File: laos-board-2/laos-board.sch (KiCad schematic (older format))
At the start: 94 parts, among them IC1 KB847, IC2 KB847, J1 USB-A, J10 CONN_4, J11 MBED NXP, J12 JP, J13 JP_3, J14 CONN_4, J15 JP, J16 JP_3, J17 POLOLU1201, J18 CONN_5, J19 JP, J2 CONN_4, J20 JP_3, J21 JP, J22 JP_3, J23 POLOLU1201, J24 CONN_5, J25 JP, J26 JP_3, J27 CONN_4, J28 JP3, J29 CONN_4, J3 JP, J30 JP, J31 JP_3, J32 POLOLU1201, J33 CONN_5, J34 CONN_4, J35 JP, J36 JP_3, J37 CONN_4, J38 CONN_2, J39 CONN_4, J4 MAGJACK, J5 CONN_2, J6 JP, J7 JP_3, J8 POLOLU1201, J9 CONN_5, Q1 TIP115, Q2 TIP115, U1 65HVD251, U2 SDCARD, U3 7805

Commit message: some more rev2 changes
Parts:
- gave numbers to parts that had none: 1
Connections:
- net GND: no longer J1.GND
- net at J11.20 (P1.31/SCK1/AD0.5), J11.24 (P2.2/PWM1.3/CTS1), J23.7 (STEP): now also J26.3 (P2)
- net at IC2.4, J11.21 (P2.5/PWM1.6/DTR1), J32.7 (STEP): now also J36.3 (P2)
- net at IC2.2, J11.22 (P2.4/PWM1.5/DSR1), J32.8 (DIR): now also J36.5 (P3)
- net at J11.23 (P2.3/PWM1.4/DCD1), J23.8 (DIR): now also J26.5 (P3)
- net at J11.26 (P2.0/PWM1.1/TXD1), J17.7 (STEP): now also J20.3 (P2)
- net at D1.2 (K), J11.7 (P0.7/SCK1/MAT2.1), J17.1 (/ENABLE)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: now also J26.1 (P1), J36.1 (P1)
- net at J31.2 (P6): now also J32.2 (MS1)
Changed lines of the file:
@@
-EESchema Schematic File Version 2  date Tue 20 Sep 2011 03:51:02 PM CEST
+EESchema Schematic File Version 2  date Wed 21 Sep 2011 02:04:42 PM CEST
 LIBS:laos_kicad_lib
 LIBS:laos-board-cache
@@
 Sheet 1 1
 Title "LAOS"
-Date "20 sep 2011"
-Rev "1"
+Date "21 sep 2011"
+Rev "2"
 Comp "http://www.laoslaser.org"
 Comment1 ""
@@
 Comment4 ""
 $EndDescr
-$Comp
-L VAA #PWR?
-U 1 1 4E7898E1
-P 11440 1440
-F 0 "#PWR?" H 11440 1500 30  0001 C CNN
-F 1 "VAA" H 11440 1550 30  0000 C CNN
-	1    11440 1440
-	1    0    0    -1
-$EndComp
+Wire Wire Line
+	7150 1020 7150 1225
+Wire Wire Line
+	12000 2600 12000 1945
+Wire Wire Line
+	11440 1435 11440 1560
+Connection ~ 9045 8625
+Wire Wire Line
+	9045 8625 9045 9150
+Wire Wire Line
+	9045 9150 10250 9150
+Wire Wire Line
+	9300 8125 8650 8125
+Connection ~ 9020 6800
+Wire Wire Line
+	9020 6800 9020 7330
+Wire Wire Line
+	9020 7330 10250 7325
+Connection ~ 9095 5050
+Wire Wire Line
+	9095 5050 9095 5575
+Wire Wire Line
+	9095 5575 10250 5575
 Connection ~ 6900 4150
 Wire Wire Line
@@
 Wire Wire Line
 	2925 3400 1650 3400
-Wire Wire Line
-	8870 6895 8870 7420
-Wire Wire Line
-	8870 7420 10245 7420
-Connection ~ 9125 6200
-Wire Wire Line
-	9125 6200 9120 7225
-Wire Wire Line
-	9120 7225 10245 7225
-Connection ~ 9095 8625
-Wire Wire Line
-	9095 8625 9095 9150
-Wire Wire Line
-	9095 9150 10255 9150
-Wire Wire Line
-	9300 8120 9295 8120
-Wire Wire Line
-	9295 8120 8655 8125
 Connection ~ 8975 3500
 Wire Wire Line
@@
 Wire Wire Line
 	8975 4030 10250 4025
-Connection ~ 9150 2800
-Wire Wire Line
-	9150 2800 9150 3820
-Wire Wire Line
-	9150 3820 10250 3820
-Connection ~ 9095 5050
-Wire Wire Line
-	9095 5050 9090 5570
-Wire Wire Line
-	9090 5570 10245 5570
 Connection ~ 7300 4450
 Wire Wire Line
@@
 Connection ~ 2000 10350
 Wire Wire Line
-	12000 1950 12000 2600
-Wire Wire Line
 	3775 10350 3900 10350
 Connection ~ 3300 10750
@@
 	1650 10750 1650 10450
 Wire Wire Line
-	7150 1025 7150 1225
-Wire Wire Line
 	12250 800  12150 800
 Wire Wire Line
@@
 Wire Wire Line
 	11350 2050 11350 2250
-Connection ~ 12000 2050
 Wire Wire Line
 	3200 10350 3475 10350
@@
 Connection ~ 9045 3400
 Wire Wire Line
-	10260 9050 9180 9050
-Wire Wire Line
-	9180 9050 9180 8025
-Connection ~ 9180 8025
-Wire Wire Line
-	10250 9245 9025 9245
-Wire Wire Line
-	9025 9245 9030 8725
-Connection ~ 9030 8725
-Wire Wire Line
-	10260 7330 8980 7330
-Wire Wire Line
-	8980 7330 8980 6800
-Connection ~ 8980 6800
-Wire Wire Line
 	8865 6905 8870 6900
-Connection ~ 8870 6900
 Wire Wire Line
 	1650 3300 3000 3300
@@
 Connection ~ 5400 770
 Wire Wire Line
-	11440 1435 11440 1560
-$Comp
-L JP J?
+	10250 7225 9105 7225
+Wire Wire Line
+	9105 7225 9105 6200
+Connection ~ 9105 6200
+Wire Wire Line
+	10250 7425 8935 7425
+Wire Wire Line
+	8935 7425 8935 6900
+Connection ~ 8935 6900
+Wire Wire Line
+	10250 9050 9130 9050
+Wire Wire Line
+	9130 9050 9130 8025
+Connection ~ 9130 8025
+Wire Wire Line
+	10250 9250 8970 9250
+Wire Wire Line
+	8970 9250 8970 8725
+Connection ~ 8970 8725
+Connection ~ 12000 2050
+Wire Wire Line
+	10255 3825 9150 3825
+Wire Wire Line
+	9150 3825 9140 2800
+Connection ~ 9140 2800
+$Comp
+L VAA #PWR57
+U 1 1 4E7898E1
+P 11440 1440
+F 0 "#PWR57" H 11440 1500 30  0001 C CNN
+F 1 "VAA" H 11440 1550 30  0000 C CNN
+	1    11440 1440
+	1    0    0    -1
+$EndComp
+$Comp
+L JP J40
 U 1 1 4E7890F5
 P 11440 1760
-F 0 "J?" H 11440 1630 60  0000 C CNN
+F 0 "J40" H 11440 1630 60  0000 C CNN
 F 1 "JP" H 11440 1875 60  0000 C CNN
 	1    11440 1760
@@
 $EndComp
 $Comp
-L VAA #PWR66
+L VAA #PWR2
 U 1 1 4E0DF8F8
 P 1650 10275
-F 0 "#PWR66" H 1650 10335 30  0001 C CNN
+F 0 "#PWR2" H 1650 10335 30  0001 C CNN
 F 1 "VAA" H 1650 10385 30  0000 C CNN
 	1    1650 10275
@@
 $EndComp
 $Comp
-L VMOT #PWR27
+L VMOT #PWR20
 U 1 1 4E0DF87E
 P 2450 3850
-F 0 "#PWR27" H 2450 3910 30  0001 C CNN
+F 0 "#PWR20" H 2450 3910 30  0001 C CNN
 F 1 "VMOT" H 2450 3960 30  0000 C CNN
 	1    2450 3850
@@
 $EndComp
 $Comp
-L VMOT #PWR21
+L VMOT #PWR46
 U 1 1 4E0DE175
 P 10300 2700
-F 0 "#PWR21" H 10300 2760 30  0001 C CNN
+F 0 "#PWR46" H 10300 2760 30  0001 C CNN
 F 1 "VMOT" H 10300 2810 30  0000 C CNN
 	1    10300 2700
@@
 $EndComp
 $Comp
-L VMOT #PWR33
+L VMOT #PWR48
 U 1 1 4E0DDF6B
 P 10300 4350
-F 0 "#PWR33" H 10300 4410 30  0001 C CNN
+F 0 "#PWR48" H 10300 4410 30  0001 C CNN
 F 1 "VMOT" H 10300 4460 30  0000 C CNN
 	1    10300 4350
@@
 $EndComp
 $Comp
-L VMOT #PWR30
+L VMOT #PWR61
 U 1 1 4E0DDF68
 P 12000 4175
-F 0 "#PWR30" H 12000 4235 30  0001 C CNN
+F 0 "#PWR61" H 12000 4235 30  0001 C CNN
 F 1 "VMOT" H 12000 4285 30  0000 C CNN
 	1    12000 4175
@@
 $EndComp
 $Comp
-L VMOT #PWR42
+L VMOT #PWR63
 U 1 1 4E0DDF1E
 P 12000 5925
-F 0 "#PWR42" H 12000 5985 30  0001 C CNN
+F 0 "#PWR63" H 12000 5985 30  0001 C CNN
 F 1 "VMOT" H 12000 6035 30  0000 C CNN
 	1    12000 5925
@@
 $EndComp
 $Comp
-L VMOT #PWR44
+L VMOT #PWR50
 U 1 1 4E0DDF1B
 P 10300 6100
-F 0 "#PWR44" H 10300 6160 30  0001 C CNN
+F 0 "#PWR50" H 10300 6160 30  0001 C CNN
 F 1 "VMOT" H 10300 6210 30  0000 C CNN
 	1    10300 6100
@@
 $EndComp
 $Comp
-L VMOT #PWR58
+L VMOT #PWR52
 U 1 1 4E0DDCF8
 P 10300 7925
-F 0 "#PWR58" H 10300 7985 30  0001 C CNN
+F 0 "#PWR52" H 10300 7985 30  0001 C CNN
 F 1 "VMOT" H 10300 8035 30  0000 C CNN
 	1    10300 7925
@@
 $EndComp
 $Comp
-L VMOT #PWR56
+L VMOT #PWR65
 U 1 1 4E0DDB84
 P 12000 7750
-F 0 "#PWR56" H 12000 7810 30  0001 C CNN
+F 0 "#PWR65" H 12000 7810 30  0001 C CNN
 F 1 "VMOT" H 12000 7860 30  0000 C CNN
 	1    12000 7750
@@
 $EndComp
 $Comp
-L VMOT #PWR14
+L VMOT #PWR59
 U 1 1 4E0DDB63
 P 12000 1950
-F 0 "#PWR14" H 12000 2010 30  0001 C CNN
+F 0 "#PWR59" H 12000 2010 30  0001 C CNN
 F 1 "VMOT" H 12000 2060 30  0000 C CNN
 	1    12000 1950
@@
 $EndComp
 $Comp
-L VAA #PWR50
+L VAA #PWR19
 U 1 1 4E0B3045
 P 2205 5570
-F 0 "#PWR50" H 2205 5630 30  0001 C CNN
+F 0 "#PWR19" H 2205 5630 30  0001 C CNN
 F 1 "VAA" H 2205 5680 30  0000 C CNN
 	1    2205 5570
@@
 $EndComp
 $Comp
-L +3V3 #PWR051
+L +3V3 #PWR050
 U 1 1 4E0B1D5E
 P 1625 775
-F 0 "#PWR051" H 1625 735 30  0001 C CNN
+F 0 "#PWR050" H 1625 735 30  0001 C CNN
 F 1 "+3V3" H 1625 885 30  0000 C CNN
 	1    1625 775
@@
 $EndComp
 $Comp
-L GND #PWR052
+L GND #PWR051
 U 1 1 4E0B1D05
 P 2175 1175
-F 0 "#PWR052" H 2175 1175 30  0001 C CNN
+F 0 "#PWR051" H 2175 1175 30  0001 C CNN
 F 1 "GND" H 2175 1105 30  0001 C CNN
 	1    2175 1175
@@
 $EndComp
 $Comp
-L GND #PWR053
+L GND #PWR052
 U 1 1 4E0B1C8A
 P 1850 2550
-F 0 "#PWR053" H 1850 2550 30  0001 C CNN
+F 0 "#PWR052" H 1850 2550 30  0001 C CNN
 F 1 "GND" H 1850 2480 30  0001 C CNN
 	1    1850 2550
@@
 $EndComp
 $Comp
-L +3V3 #PWR054
+L +3V3 #PWR053
 U 1 1 4E0B1449
 P 2050 4850
-F 0 "#PWR054" H 2050 4810 30  0001 C CNN
+F 0 "#PWR053" H 2050 4810 30  0001 C CNN
 F 1 "+3V3" H 2050 4960 30  0000 C CNN
 	1    2050 4850
@@
 $EndComp
 $Comp
-L GND #PWR055
+L GND #PWR054
 U 1 1 4E0B1431
 P 1850 5600
-F 0 "#PWR055" H 1850 5600 30  0001 C CNN
+F 0 "#PWR054" H 1850 5600 30  0001 C CNN
 F 1 "GND" H 1850 5530 30  0001 C CNN
 	1    1850 5600
@@
 $EndComp
 $Comp
-L GND #PWR056
+L GND #PWR055
 U 1 1 4E0B0CE0
 P 1850 3550
-F 0 "#PWR056" H 1850 3550 30  0001 C CNN
+F 0 "#PWR055" H 1850 3550 30  0001 C CNN
 F 1 "GND" H 1850 3480 30  0001 C CNN
 	1    1850 3550
@@
 $EndComp
 $Comp
-L +5V #PWR057
+L +5V #PWR056
 U 1 1 4E0B068F
 P 3300 10275
-F 0 "#PWR057" H 3300 10365 20  0001 C CNN
+F 0 "#PWR056" H 3300 10365 20  0001 C CNN
 F 1 "+5V" H 3300 10365 30  0000 C CNN
 	1    3300 10275
@@
 $EndComp
 $Comp
-L GND #PWR058
+L GND #PWR057
 U 1 1 4E0B060C
 P 2800 10775
-F 0 "#PWR058" H 2800 10775 30  0001 C CNN
+F 0 "#PWR057" H 2800 10775 30  0001 C CNN
 F 1 "GND" H 2800 10705 30  0001 C CNN
 	1    2800 10775

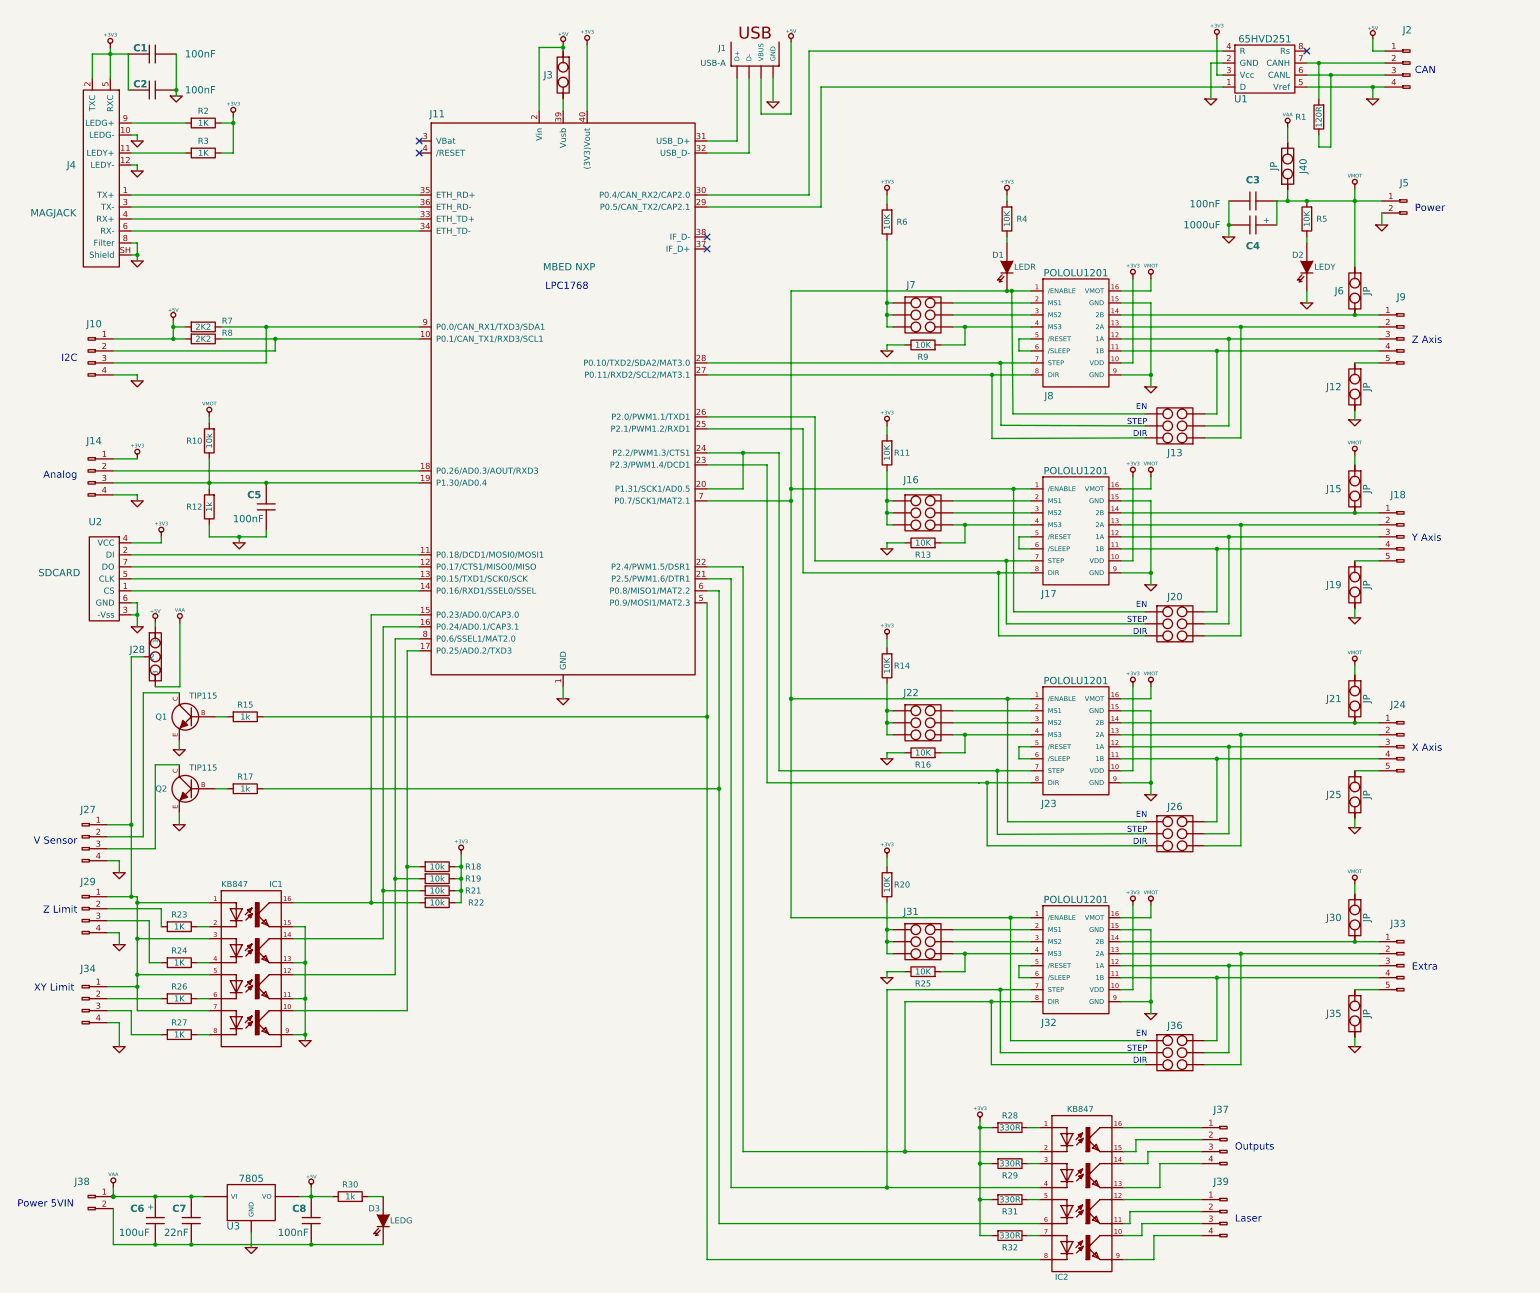
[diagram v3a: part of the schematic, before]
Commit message: - Checked schematic - Added connector values and pin text - made pin selection for transistor outputs - Made pull-up resistor values 1K.
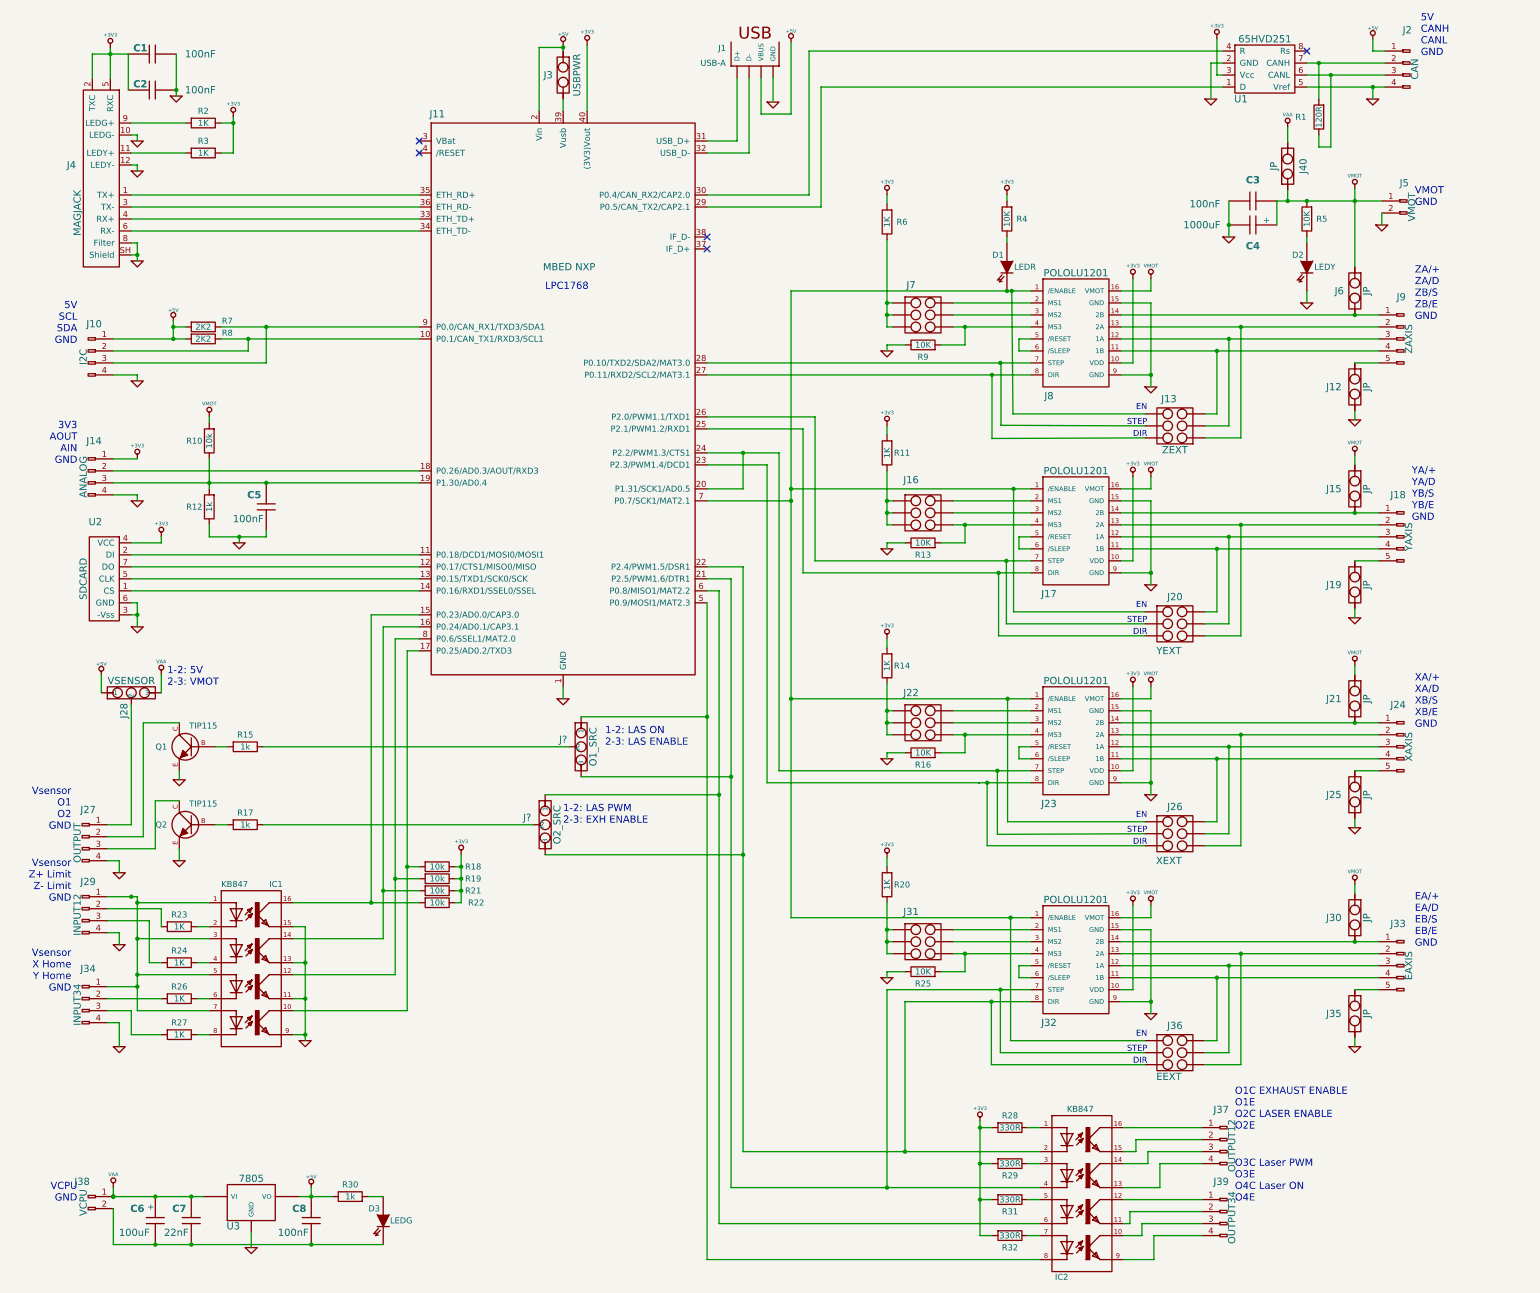
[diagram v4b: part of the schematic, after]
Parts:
- added J?: O1_SRC, symbol JP3
- added J?: O2_SRC, symbol JP3
- J10: value CONN_4 -> I2C
- J13: value JP_3 -> ZEXT
- J14: value CONN_4 -> ANALOG
- J18: value CONN_5 -> YAXIS
- J2: value CONN_4 -> CAN
- J20: value JP_3 -> YEXT
- J24: value CONN_5 -> XAXIS
- J26: value JP_3 -> XEXT
- J27: value CONN_4 -> OUTPUT
- J28: value JP3 -> VSENSOR
- J29: value CONN_4 -> INPUT12
- J3: value JP -> USBPWR
- J33: value CONN_5 -> EAXIS
- J34: value CONN_4 -> INPUT34
- J36: value JP_3 -> EEXT
- J37: value CONN_4 -> OUTPUT12
- J38: value CONN_2 -> VCPU
- J39: value CONN_4 -> OUTPUT34
- J5: value CONN_2 -> VMOT
- J9: value CONN_5 -> ZAXIS
- R11, R14, R20, R6: value 10K -> 1K
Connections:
- net at IC2.4, J11.21 (P2.5/PWM1.6/DTR1), J32.7 (STEP)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: now also J?.3
- net at IC2.2, J11.22 (P2.4/PWM1.5/DSR1), J32.8 (DIR)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: now also J?.3
- net at IC2.8, J11.5 (P0.9/MOSI1/MAT2.3): now also J?.1; no longer R15.1
- net at IC2.6, J11.6 (P0.8/MISO1/MAT2.2): now also J?.1; no longer R17.1
- net at IC1.1, IC1.3 (A), IC1.5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: no longer J27.1 (P1), J28.2
- new net: J27.1 (P1), J28.2
- new net: J?.2, R17.1
- new net: J?.2, R15.1
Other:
- note added: "1-2: 5V\n2-3: VMOT"
- note added: "1-2: LAS ON\n2-3: LAS ENABLE"
- note added: "1-2: LAS PWM\n2-3: EXH ENABLE"
- note added: "3V3\nAOUT\nAIN\nGND"
- note added: "5V\nCANH\nCANL\nGND"
- note added: "5V\nSCL\nSDA\nGND"
- note added: "EA/+\nEA/D\nEB/S\nEB/E\nGND"
- note added: "O1C EXHAUST ENABLE\nO1E\nO2C LASER ENABLE\nO2E"
- note added: "O3C Laser PWM\nO3E \nO4C Laser ON\nO4E"
- note added: "VCPU\nGND"
- note added: "VMOT\nGND"
- note added: "Vsensor\nO1\nO2\nGND"
- note added: "Vsensor\nX Home\nY Home\nGND"
- note added: "Vsensor\nZ+ Limit\nZ- Limit\nGND\n"
- note added: "XA/+\nXA/D\nXB/S\nXB/E\nGND"
- note added: "YA/+\nYA/D\nYB/S\nYB/E\nGND"
- note added: "ZA/+\nZA/D\nZB/S\nZB/E\nGND"
- note removed: "Analog"
- note removed: "CAN"
- note removed: "Extra"
- note removed: "I2C"
- note removed: "Laser"
- note removed: "Outputs"
- note removed: "Power"
- note removed: "Power 5VIN"
- note removed: "V Sensor"
- note removed: "X Axis"
- note removed: "XY Limit"
- note removed: "Y Axis"
- note removed: "Z Axis"
- note removed: "Z Limit"
- moved on the sheet: J28, Q1, Q2, R15, R17
